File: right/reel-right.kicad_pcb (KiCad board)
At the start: 2 copper layers, 134 x 87.3 mm, 42 parts, among them J1 Conn_01x02, SW1 SW_Push, SW10 SW_Push, SW11 SW_Push, SW12 SW_Push, SW13 SW_Push, SW14 SW_Push, SW15 SW_Push, SW16 SW_Push, SW17 SW_Push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

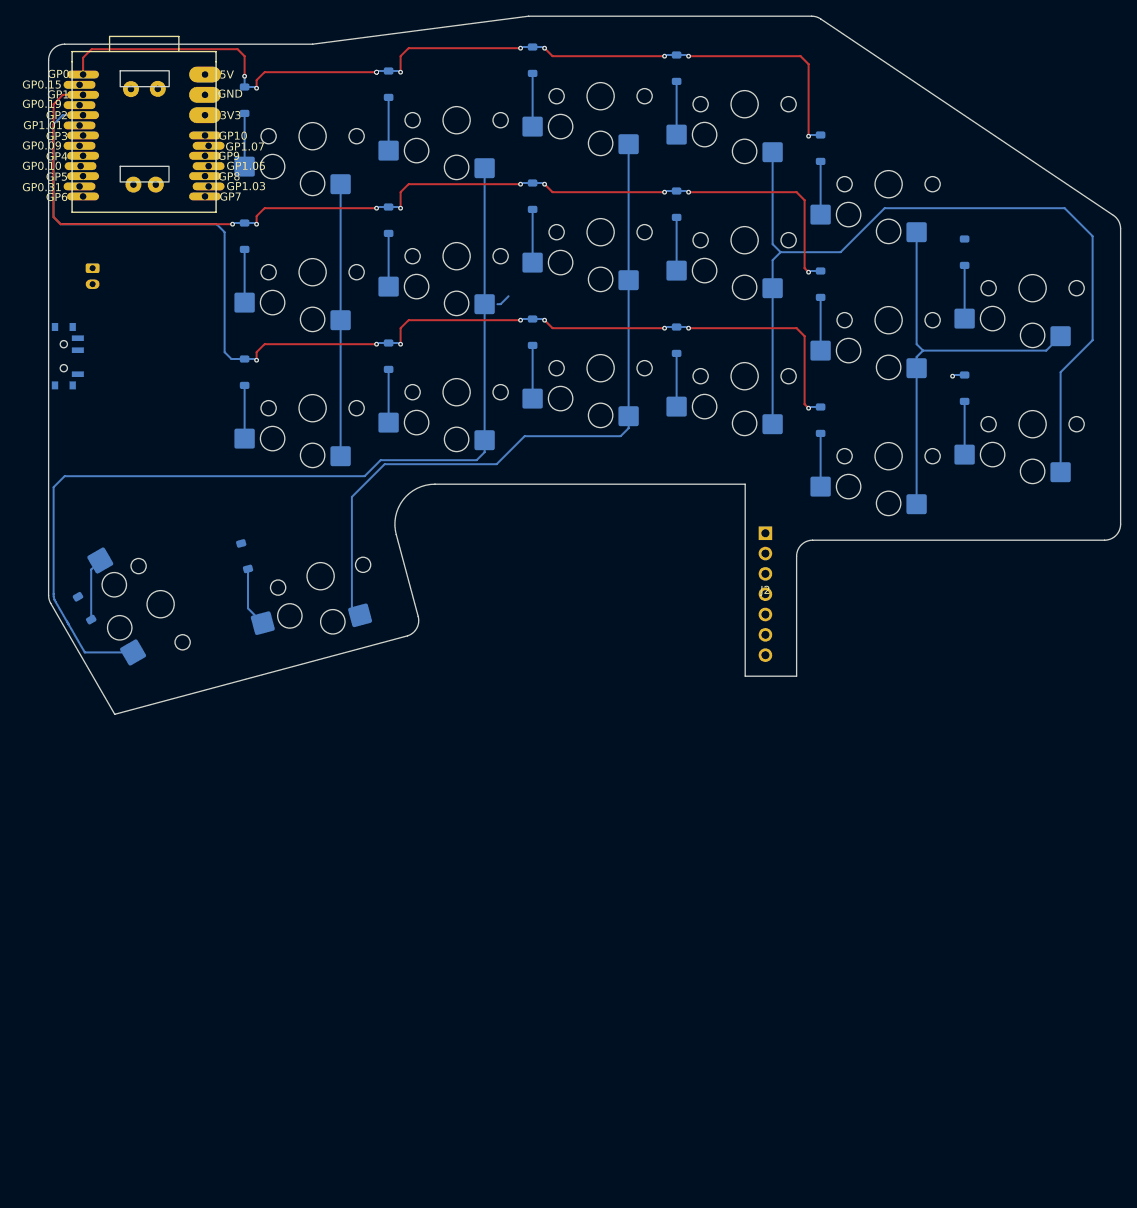
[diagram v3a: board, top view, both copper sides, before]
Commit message: Update right PCB layout
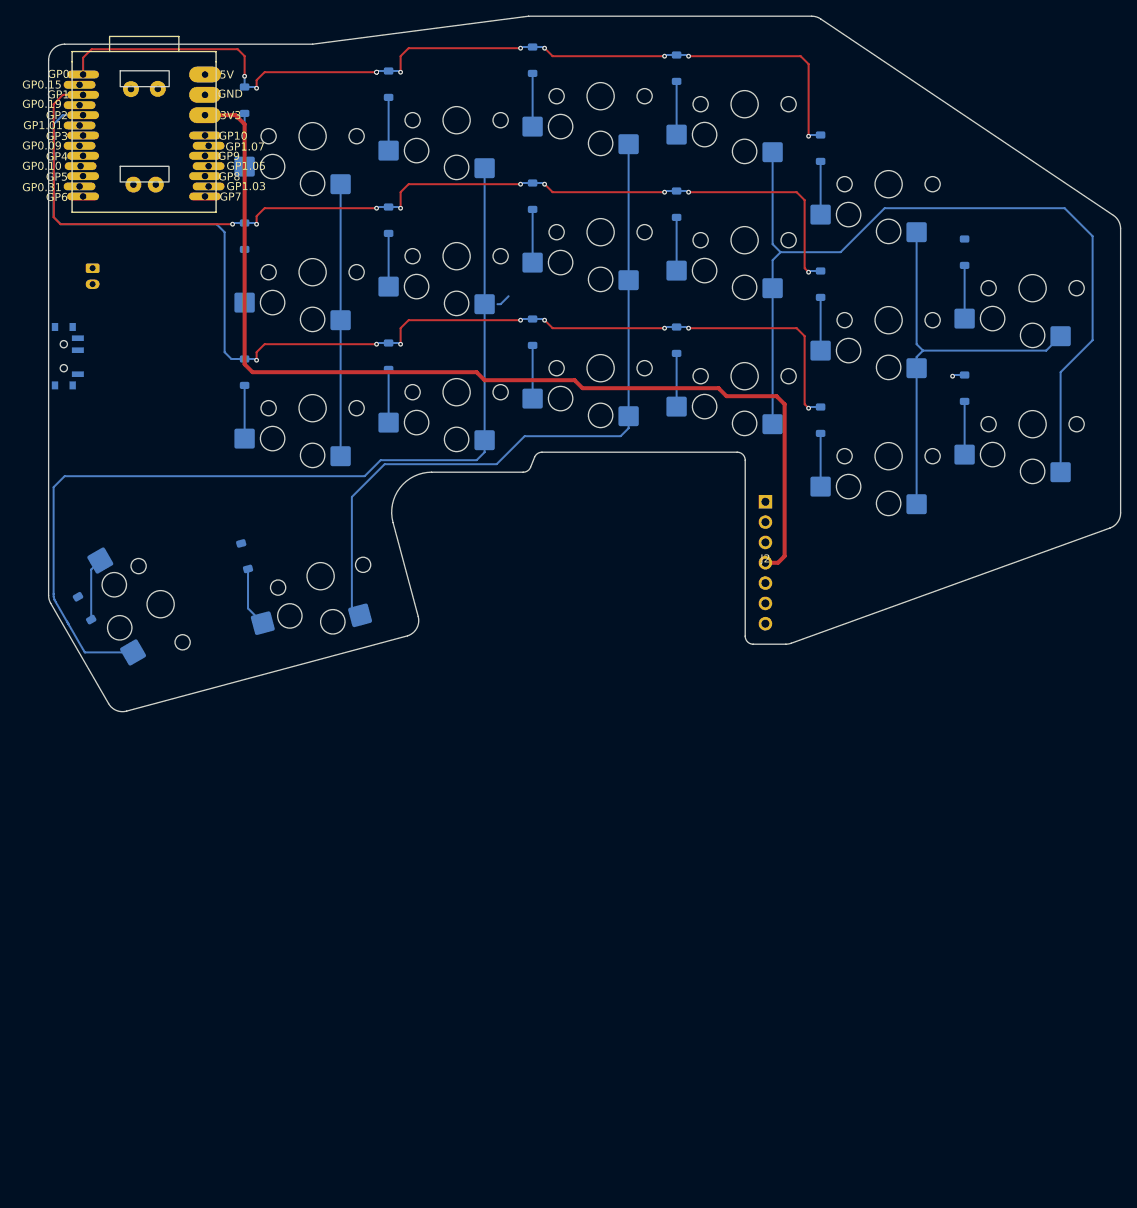
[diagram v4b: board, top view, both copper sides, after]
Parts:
- moved J2 3.93 mm to (136.6, 113.8)
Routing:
- net 3.3V: track 0.00 -> 126.7 mm
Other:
- board size 134 x 87.3 mm -> 134 x 86.9 mm
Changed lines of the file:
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@@
 		(capping no)
 		(filling no)
-		(zone_defaults)
 		(pcbplotparams
 			(layerselection 0x00000000_00000000_55555555_5755f5ff)
@@
 	(footprint "reel:pmw3610_connector"
 		(layer "F.Cu")
-		(at 136.6 117.75)
+		(at 136.6 113.82)
 		(property "Reference" "J2"
 			(at 0 -0.5 0)
@@
 	(gr_line
 		(start 47.267949 118.901924)
-		(end 55.270834 132.763327)
+		(end 54.503472 131.434154)
 		(stroke
 			(width 0.05)
@@
 		(layer "Edge.Cuts")
 	)
+	(gr_arc
+		(start 56.753158 132.366002)
+		(mid 55.470155 132.28191)
+		(end 54.503472 131.434154)
+		(stroke
+			(width 0.05)
+			(type default)
+		)
+		(layer "Edge.Cuts")
+	)
 	(gr_line
 		(start 80 49)
@@
 	)
 	(gr_line
-		(start 90.454447 110.294095)
+		(start 90.052523 108.794095)
 		(end 93.19777 120.532314)
 		(stroke
@@
 	)
 	(gr_arc
-		(start 90.454447 110.294095)
-		(mid 91.31731 105.956186)
-		(end 95.284076 104)
+		(start 90.052523 108.794095)
+		(mid 90.915386 104.456193)
+		(end 94.882152 102.5)
 		(stroke
 			(width 0.05)
@@
 	(gr_line
 		(start 91.871403 122.956097)
-		(end 55.2708 132.763199)
+		(end 56.753158 132.366002)
 		(stroke
 			(width 0.05)
@@
 	)
 	(gr_line
+		(start 94.882152 102.5)
+		(end 106.322967 102.5)
+		(stroke
+			(width 0.05)
+			(type default)
+		)
+		(layer "Edge.Cuts")
+	)
+	(gr_line
 		(start 107 45.5)
 		(end 80 49)
@@
 		(layer "Edge.Cuts")
 	)
-	(gr_line
-		(start 134.075 104)
-		(end 95.284076 104)
+	(gr_arc
+		(start 107.251444 101.871391)
+		(mid 106.883596 102.328068)
+		(end 106.322967 102.5)
 		(stroke
 			(width 0.05)
@@
 	)
 	(gr_line
-		(start 134.075 128)
-		(end 134.075 104)
+		(start 107.251444 101.871391)
+		(end 107.748556 100.62861)
 		(stroke
 			(width 0.05)
-			(type solid)
+			(type default)
+		)
+		(layer "Edge.Cuts")
+	)
+	(gr_arc
+		(start 107.748556 100.62861)
+		(mid 108.116407 100.171946)
+		(end 108.677033 100)
+		(stroke
+			(width 0.05)
+			(type default)
 		)
 		(layer "Edge.Cuts")
 	)
 	(gr_line
-		(start 134.075 128)
-		(end 140.5 128)
+		(start 133.075 100)
+		(end 108.677033 100)
 		(stroke
 			(width 0.05)
@@
 	)
 	(gr_arc
-		(start 140.5 113)
-		(mid 141.085786 111.585786)
-		(end 142.5 111)
+		(start 133.075 100)
+		(mid 133.782107 100.292893)
+		(end 134.075 101)
 		(stroke
 			(width 0.05)
@@
 	)
 	(gr_line
-		(start 140.5 128)
-		(end 140.5 113)
+		(start 134.075 123)
+		(end 134.075 101)
+		(stroke
+			(width 0.05)
+			(type solid)
+		)
+		(layer "Edge.Cuts")
+	)
+	(gr_arc
+		(start 135.075 124)
+		(mid 134.367893 123.707107)
+		(end 134.075 123)
+		(stroke
+			(width 0.05)
+			(type default)
+		)
+		(layer "Edge.Cuts")
+	)
+	(gr_line
+		(start 135.075 124)
+		(end 139.149646 124)
 		(stroke
 			(width 0.05)
@@
 	)
 	(gr_arc
-		(start 142.391139 45.5)
-		(mid 142.973609 45.586695)
-		(end 143.505577 45.839269)
+		(start 139.829492 123.880907)
+		(mid 139.494746 123.97001)
+		(end 139.149646 124)
 		(stroke
 			(width 0.05)
@@
 	)
 	(gr_line
-		(start 179 111)
-		(end 142.5 111)
+		(start 139.829492 123.880907)
+		(end 179.679846 109.477164)
+		(stroke
+			(width 0.05)
+			(type default)
+		)
+		(layer "Edge.Cuts")
+	)
+	(gr_arc
+		(start 142.391139 45.5)
+		(mid 142.973609 45.586695)
+		(end 143.505577 45.839269)
 		(stroke
 			(width 0.05)
@@
 	(gr_line
 		(start 181 72.066472)
-		(end 181 109)
+		(end 181 107.596258)
 		(stroke
 			(width 0.05)
@@
 	)
 	(gr_arc
-		(start 181 109)
-		(mid 180.414214 110.414214)
-		(end 179 111)
+		(start 181 107.596258)
+		(mid 180.637024 108.745237)
+		(end 179.679846 109.477164)
 		(stroke
 			(width 0.05)
@@
 	)
 	(segment
+		(start 139 113)
+		(end 139 94)
+		(width 0.5)
+		(layer "F.Cu")
+		(net "3.3V")
+	)
+	(segment
+		(start 130.75 92)
+		(end 113.75 92)
+		(width 0.5)
+		(layer "F.Cu")
+		(net "3.3V")
+	)
+	(segment
+		(start 136.6 113.82)
+		(end 138.18 113.82)
+		(width 0.5)
+		(layer "F.Cu")
+		(net "3.3V")
+	)
+	(segment
+		(start 71.5 59)
+		(end 70.37 57.87)
+		(width 0.5)
+		(layer "F.Cu")
+		(net "3.3V")
+	)
+	(segment
+		(start 100.5 90)
+		(end 72.5 90)
+		(width 0.5)
+		(layer "F.Cu")
+		(net "3.3V")
+	)
+	(segment
+		(start 71.5 89)
+		(end 71.5 59)
+		(width 0.5)
+		(layer "F.Cu")
+		(net "3.3V")
+	)
+	(segment
+		(start 101.5 91)
+		(end 100.5 90)
+		(width 0.5)
+		(layer "F.Cu")
+		(net "3.3V")
+	)
+	(segment
+		(start 112.75 91)
+		(end 101.5 91)
+		(width 0.5)
+		(layer "F.Cu")
+		(net "3.3V")
+	)
+	(segment
+		(start 70.37 57.87)
+		(end 66.55 57.87)
+		(width 0.5)
+		(layer "F.Cu")
+		(net "3.3V")
+	)
+	(segment
+		(start 113.75 92)
+		(end 112.75 91)
+		(width 0.5)
+		(layer "F.Cu")
+		(net "3.3V")
+	)
+	(segment
+		(start 72.5 90)
+		(end 71.5 89)
+		(width 0.5)
+		(layer "F.Cu")
+		(net "3.3V")
+	)
+	(segment
+		(start 138 93)
+		(end 131.75 93)
+		(width 0.5)
+		(layer "F.Cu")
+		(net "3.3V")
+	)
+	(segment
+		(start 139 94)
+		(end 138 93)
+		(width 0.5)
+		(layer "F.Cu")
+		(net "3.3V")
+	)
+	(segment
+		(start 138.18 113.82)
+		(end 139 113)
+		(width 0.5)
+		(layer "F.Cu")
+		(net "3.3V")
+	)
+	(segment
+		(start 131.75 93)
+		(end 130.75 92)
+		(width 0.5)
+		(layer "F.Cu")
+		(net "3.3V")
+	)
+	(segment
